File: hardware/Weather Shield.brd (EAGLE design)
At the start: 53.3 x 59.7 mm, 50 parts, among them Q1 BSS138, Q2 BSS138, U1 ARDUINO_R3_SHIELD, U2 3.3V MIC5219, U3 ALS-PT19, U4 MPL3115A2LGA8, U5 HTU21D, U7 GP-635T, U8 TEMT6000

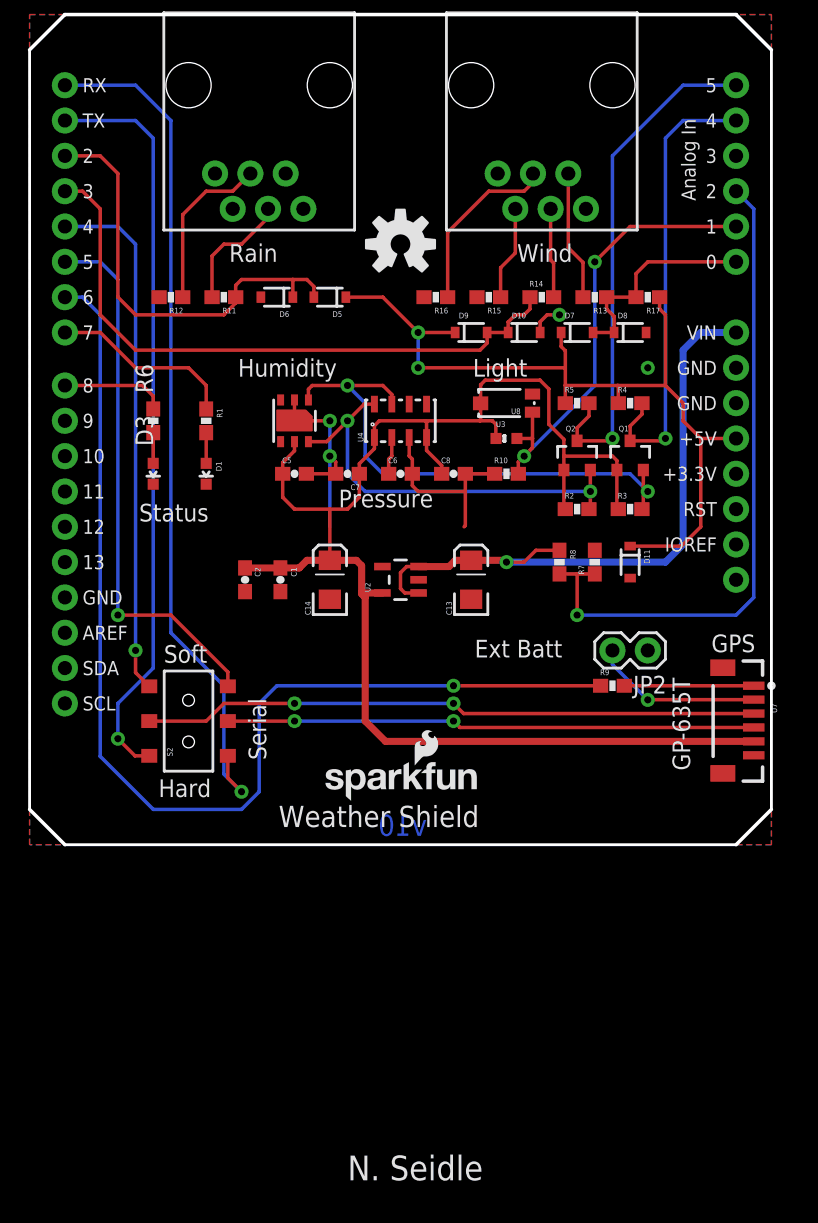
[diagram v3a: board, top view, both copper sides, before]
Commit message: v1.1 that addresses many issues.
Many schematic and routing changes. See issues.
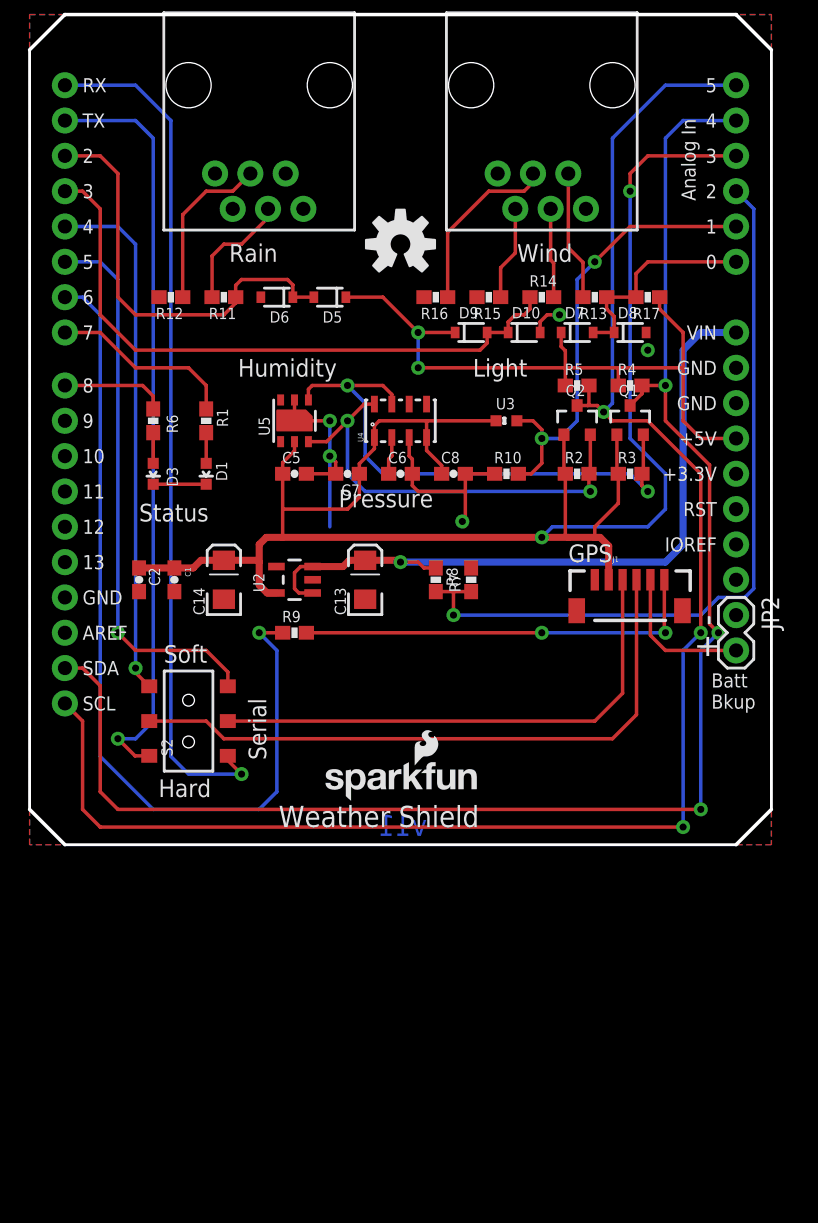
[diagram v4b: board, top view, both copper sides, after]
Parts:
- removed D11: 3.6V, SparkFun:SOD-323
- removed U7: GP-635T, SparkFun-Connectors:JST-6-SMD-VERT-1.0MM
- removed U8: TEMT6000, SparkFun-Sensors:TEMT6000-SEN
- added J1: GP-635T, SparkFun-Sensors:GP-635T
- JP2: value M02PTH -> External Batt Bckup
- moved R9 23.2 mm to (19.1, 15.2)
- moved R7 8.98 mm to (31.8, 19.1)
- moved R8 8.98 mm to (29.2, 19.1)
- moved C13 7.62 mm to (24.1, 19.1)
- moved U2 7.62 mm to (19.1, 19.1)
- moved C2 7.62 mm to (7.87, 19.1)
- moved C1 7.62 mm to (10.4, 19.1)
- moved C14 7.62 mm to (14.0, 19.1)
- moved JP2 6.84 mm to (50.8, 16.5), turned to 270 degrees
- moved R2 2.54 mm to (39.4, 26.7)
- moved R3 2.54 mm to (43.2, 26.7)
- moved Q1 2.54 mm to (43.2, 30.5)
- moved Q2 2.54 mm to (39.4, 30.5)
- moved R4 1.27 mm to (43.2, 33.0)
- moved R5 1.27 mm to (39.4, 33.0)
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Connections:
- net 3.3V: now also J1.2, U1.A3; no longer U7.5, U8.COLLECTOR
- net 3V_PWR_CTL: now also J1.6; no longer U7.1
- net 5V: no longer D11.1
- net GND: now also J1.1; no longer D11.2, U7.6
- net GPS-RX: now also J1.4; no longer U7.3
- net GPS-TX: now also J1.3; no longer U7.4
- net HV_SCL: now also U1.SCL
- net HV_SDA: now also U1.SDA
- net LIGHT: no longer U8.EMITTER
- net V_BATT: now also J1.5; no longer U7.2
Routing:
- net HV_SCL: track 37.0 -> 120.6 mm, vias 1 -> 3
- net HV_SDA: track 32.9 -> 113.8 mm, vias 1 -> 3
- net 3.3V: track 108.8 -> 131.9 mm, vias 0 -> 2
- net 3V_PWR_CTL: track 9.31 -> 29.7 mm, vias 0 -> 2
- net PWR_CTL: track 79.8 -> 63.3 mm
- net 5V: track 61.7 -> 49.7 mm
- net BATT_LVL: track 48.5 -> 55.7 mm
- net RAW: track 46.3 -> 52.5 mm
- net GND: track 31.1 -> 34.9 mm, vias 4 -> 5
- net GPS-RX: track 44.3 -> 46.0 mm, vias 2 -> 0
- net V_BATT: track 12.2 -> 10.6 mm, vias 1 -> 0
- net SCL: track 30.5 -> 31.8 mm
- net RAIN: track 31.9 -> 30.7 mm
- net SDA: track 37.9 -> 39.1 mm
- net TXO: track 53.9 -> 54.6 mm
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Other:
- board text added: "+"
- board text added: "-"
- board text added: "Batt Bkup"
- board text added: "v11"
- board text removed: "Ext Batt"
- board text removed: "GP-635T"
- board text removed: "v10"

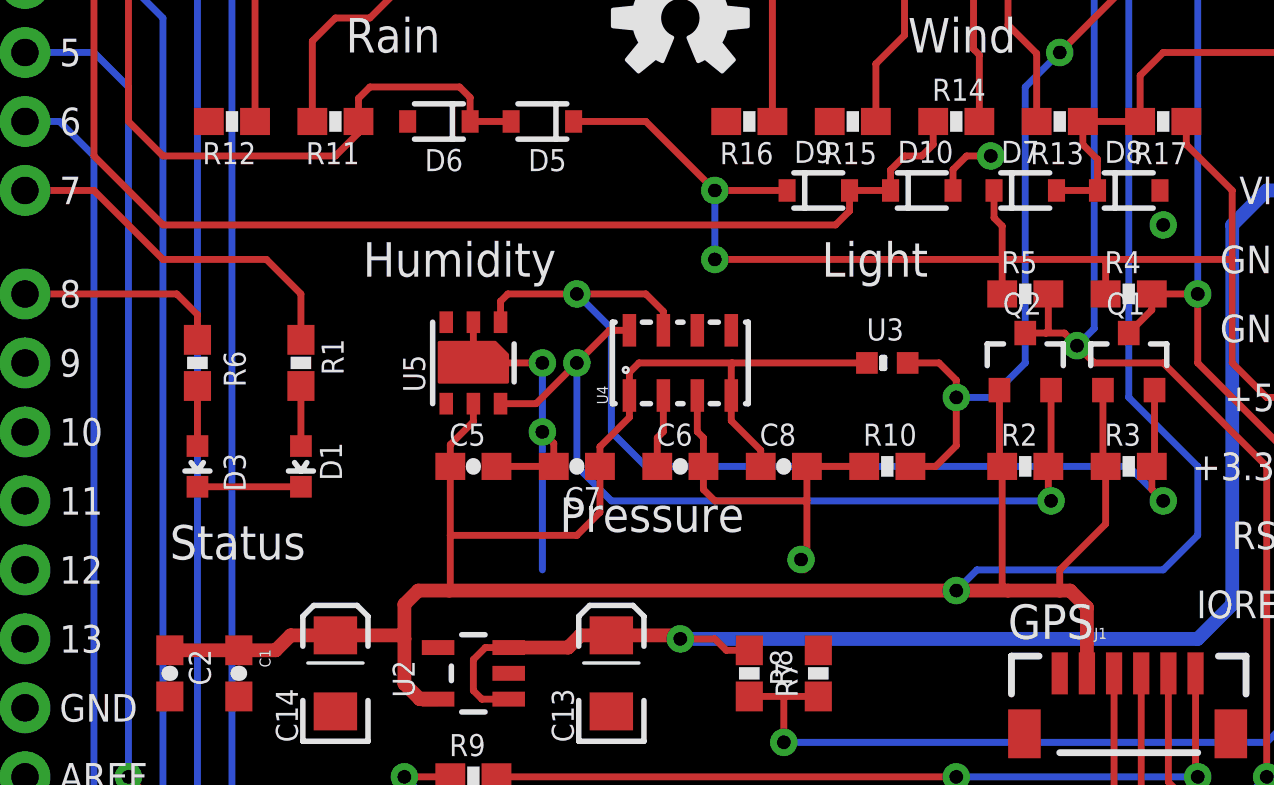
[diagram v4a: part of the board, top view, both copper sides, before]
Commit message: Added milling slots and updated readme.
Added slots to allow better airflow around sensors.
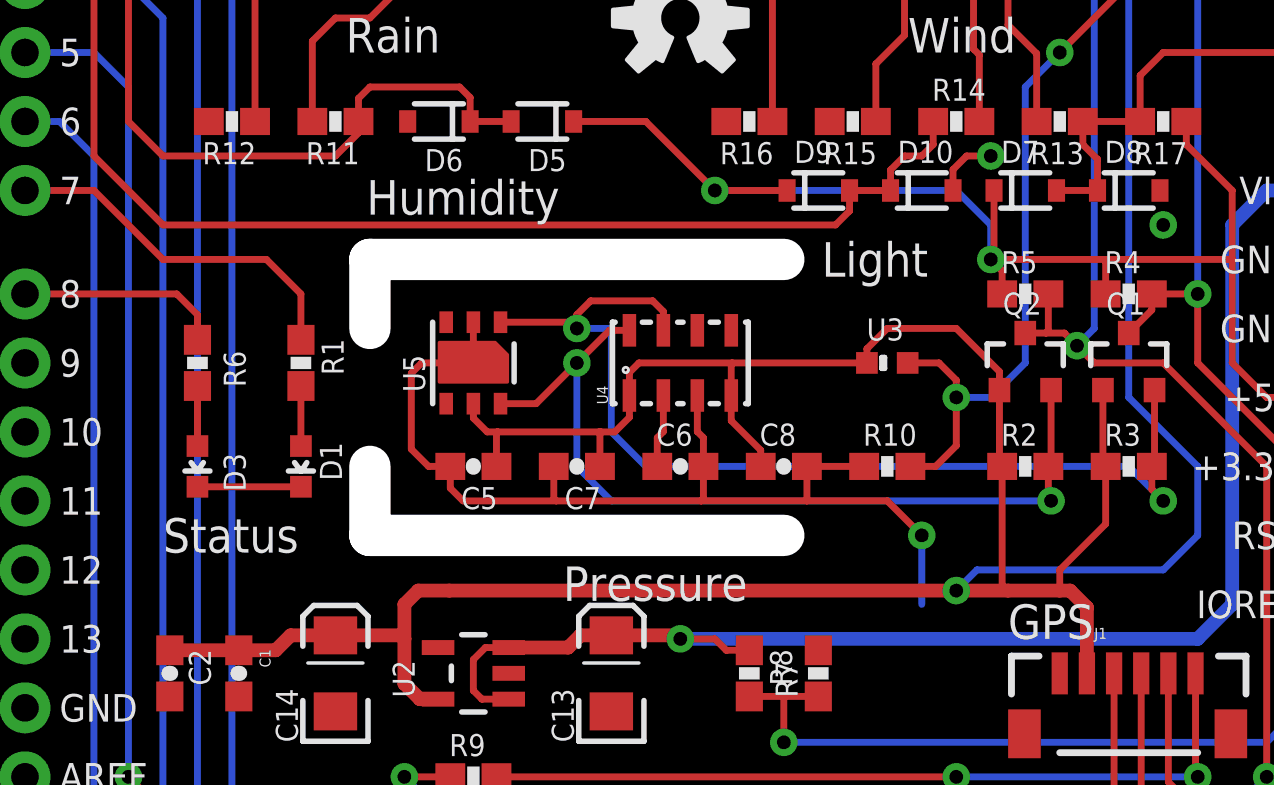
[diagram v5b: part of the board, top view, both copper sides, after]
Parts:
- turned C5 to 180 degrees
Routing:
- net GND: track 34.9 -> 44.7 mm, vias 5 -> 3
- net SDA: track 39.1 -> 38.4 mm
- net 3.3V: track 131.9 -> 131.2 mm
- net 5V: track 49.7 -> 49.1 mm
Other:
- outline, holes or cut-outs redrawn
